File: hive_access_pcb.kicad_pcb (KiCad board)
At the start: 2 copper layers, 43 parts, among them J1 Door Reader, J2 Snub Enable, J3 Relay Mode Select, J4 Relay Voltage Select, J5 Power In, J6 Exit Sensor, K1 SANYOU_SRD_Form_C, P1 Door Latch Solenoid Out, P2 External Reset, P3 Door Closed Sensor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

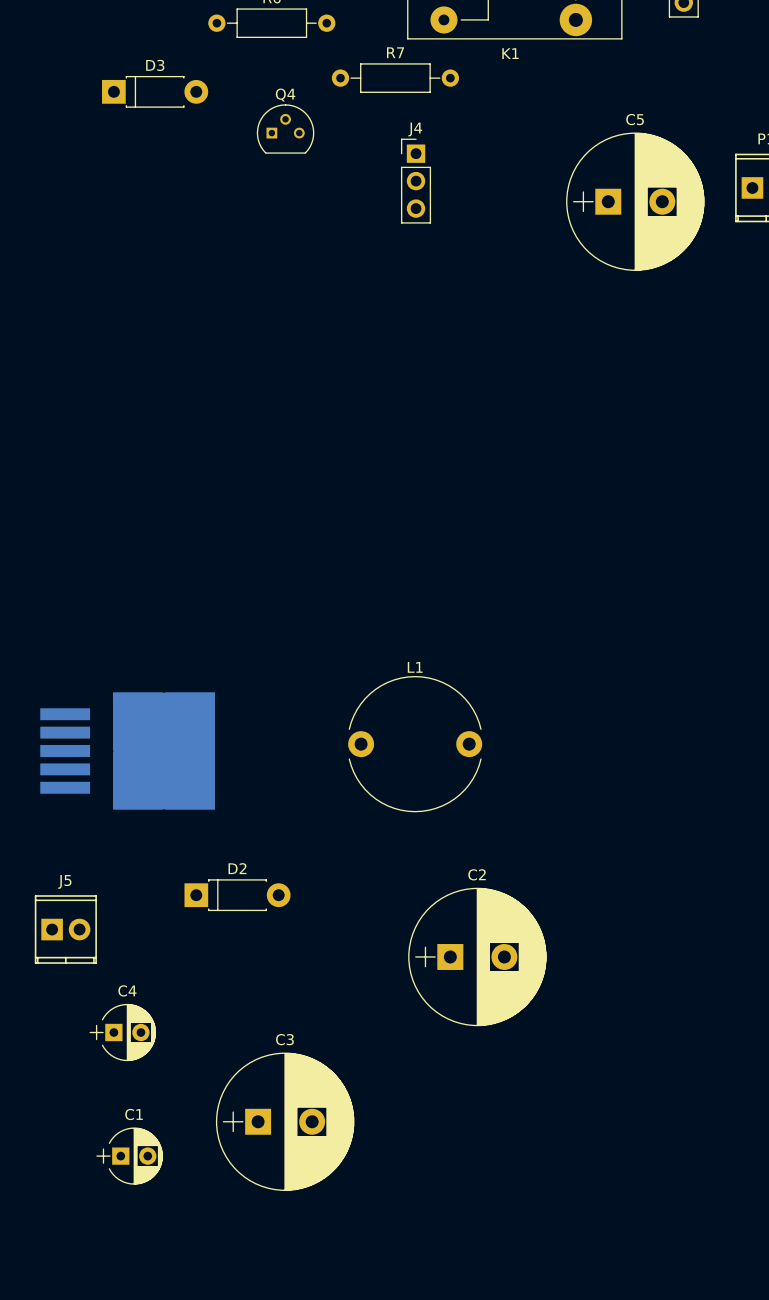
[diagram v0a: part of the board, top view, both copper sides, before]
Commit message: All components correctly sized, except connectors.  Need to check TO-92 pinouts.
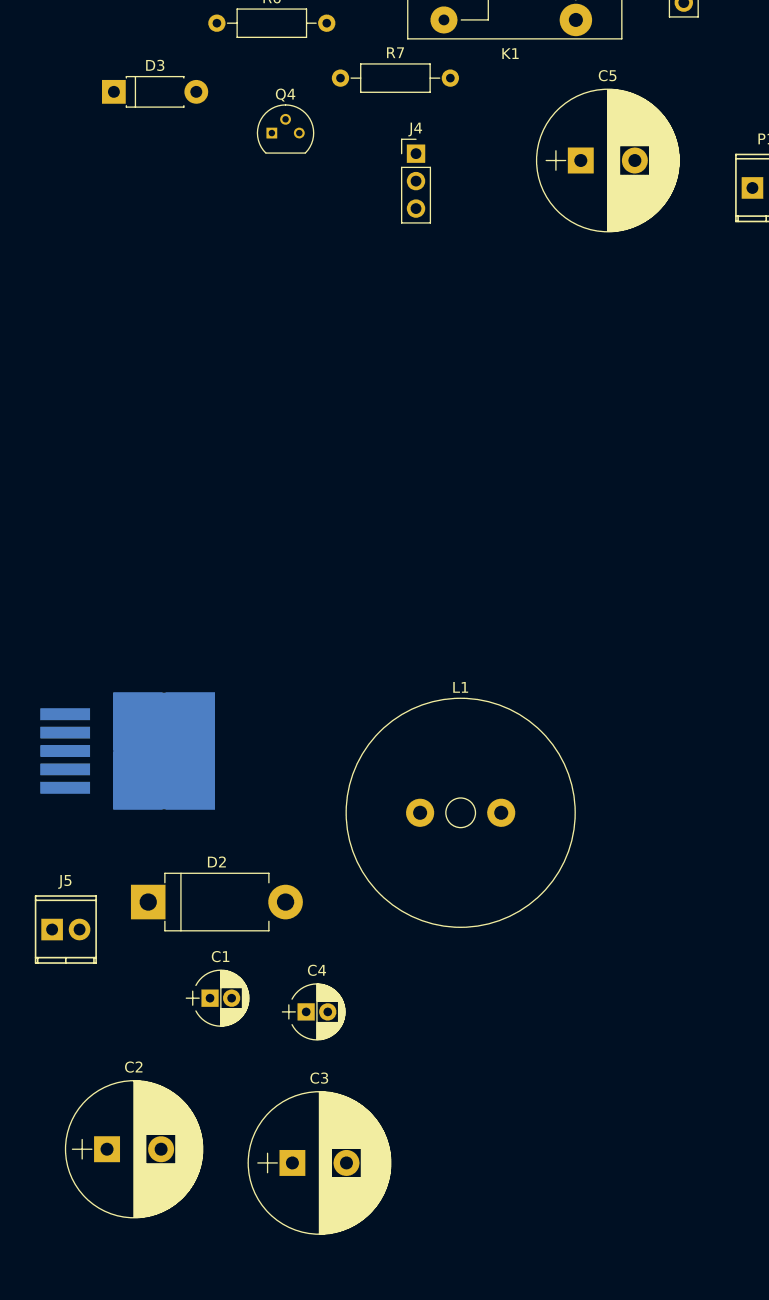
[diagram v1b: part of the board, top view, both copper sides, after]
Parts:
- C1, C4: footprint Capacitors_THT:CP_Radial_D5.0mm_P2.50mm -> Capacitors_THT:CP_Radial_D5.0mm_P2.00mm
- C3, C5: footprint Capacitors_THT:CP_Radial_D12.5mm_P5.00mm -> Capacitors_THT:CP_Radial_D13.0mm_P5.00mm
- D2: footprint Diodes_THT:D_DO-41_SOD81_P7.62mm_Horizontal -> Diodes_THT:D_DO-201AD_P12.70mm_Horizontal
- L1: footprint Inductors_THT:L_Radial_D12.0mm_P10.00mm_Neosid_SD12_style1 -> Inductor:L_Radial_D21.0mm_P7.5mm
- moved C2 36.4 mm to (191.1, 141.0)
- moved C4 17.9 mm to (209.6, 128.3)
- moved C1 16.8 mm to (200.7, 127.0)
- moved L1 6.63 mm to (216.5, 109.9)
- moved C3 4.96 mm to (208.3, 142.2)
- moved C5 4.58 mm to (234.9, 49.5)
- moved D2 4.49 mm to (194.9, 118.1)

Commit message: First draft of the circuit board.
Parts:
- moved J1 193.5 mm to (233.7, 55.9), turned to 180 degrees
- moved R5 192.4 mm to (252.7, 72.4), turned to 180 degrees
- moved R4 192.4 mm to (252.7, 77.5), turned to 180 degrees
- moved C6 187.7 mm to (221.6, 65.4)
- moved R1 186.2 mm to (228.6, 77.5)
- moved R2 184.8 mm to (228.6, 72.4)
- moved Q3 181.9 mm to (240.7, 66.0)
- moved U3 175.2 mm to (222.2, 75.6)
- moved Q2 174.5 mm to (233.0, 66.0)
- moved R9 160.8 mm to (230.5, 118.7), turned to 270 degrees
- moved P2 152.1 mm to (239.4, 137.2)
- moved U4 150.3 mm to (237.5, 99.7)
- moved U2 148.5 mm to (238.1, 125.1), turned to 90 degrees
- moved P3 106.6 mm to (216.5, 64.8), turned to 180 degrees
- moved J3 92.5 mm to (166.4, 76.8), turned to 270 degrees
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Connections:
- U3 pad 13: /WIEGAND_BEEP -> /WIEGAND_LIGHT
- U3 pad 14: /WIEGAND_LIGHT -> /WIEGAND_BEEP
- U4 pad 5: /WEMOS_D1 -> /WEMOS_D0
- U4 pad 6: /WEMOS_D0 -> /WEMOS_D1
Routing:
- net GND: track 0.00 -> 525.7 mm, vias 0 -> 12
- net +5V: track 0.00 -> 287.2 mm, vias 0 -> 4
- net +12V: track 0.00 -> 245.2 mm, vias 0 -> 4
- net +3V3: track 0.00 -> 223.4 mm, vias 0 -> 6
- net /ONE_WIRE: track 0.00 -> 104.4 mm, vias 0 -> 2
- net /WEMOS_TRIG: track 0.00 -> 87.2 mm
- net /WEMOS_ECHO: track 0.00 -> 75.5 mm
- net /~RST: track 0.00 -> 59.1 mm
- net /RELAY_POWER: track 0.00 -> 44.4 mm
- net /HC_TRIG: track 0.00 -> 42.1 mm
- net /WEMOS_D1: track 0.00 -> 42.0 mm
- net /DOOR_SENSOR: track 0.00 -> 41.8 mm
- net /WEMOS_D0: track 0.00 -> 40.7 mm
- net /RELAY_CONN: track 0.00 -> 37.8 mm
- net /WIEGAND_D1: track 0.00 -> 35.6 mm
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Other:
- net class Default: clearance 0.2 -> 0.2032; trace_width 0.25 -> 0.254; via_dia 0.6 -> 2.54; via_drill 0.4 -> 1.27
- net class Lesser Power added: clearance 0.2032, trace_width 1.016, via_dia 1.905, via_drill 1.016
- net class Power added: clearance 0.2032, trace_width 1.524, via_dia 1.905, via_drill 1.016
- rule trace_clearance: 0.2 -> 0.2032

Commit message: Design rule tweaks.
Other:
- board outline added: 139.1 x 111.8 mm
- net class Default: clearance 0.2032 -> 0.2286; via_dia 2.54 -> 1.905; via_drill 1.27 -> 1.016
- net class Lesser Power: clearance 0.2032 -> 0.2286
- net class Power: clearance 0.2032 -> 0.2286; via_dia 1.905 -> 2.286; via_drill 1.016 -> 1.27
- rule trace_clearance: 0.2032 -> 0.2286
- rule trace_min: 0.2 -> 0.2032
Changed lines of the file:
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@@
     (area 0 0 0 0)
     (thickness 1.6)
-    (drawings 0)
-    (tracks 462)
+    (drawings 4)
+    (tracks 464)
     (zones 0)
     (modules 43)
@@
     (user_trace_width 0.635)
     (user_trace_width 1.1176)
-    (trace_clearance 0.2032)
+    (trace_clearance 0.2286)
     (zone_clearance 0.508)
     (zone_45_only no)
-    (trace_min 0.2)
+    (trace_min 0.2032)
     (segment_width 0.2)
     (edge_width 0.15)
-    (via_size 2.54)
-    (via_drill 1.27)
+    (via_size 1.905)
+    (via_drill 1.016)
     (via_min_size 0.4)
     (via_min_drill 0.3)
@@
   (net 41 "Net-(K1-Pad3)")
   (net_class Default "This is the default net class."
-    (clearance 0.2032)
+    (clearance 0.2286)
     (trace_width 0.254)
-    (via_dia 2.54)
-    (via_drill 1.27)
+    (via_dia 1.905)
+    (via_drill 1.016)
     (uvia_dia 0.3)
     (uvia_drill 0.1)
@@
   )
   (net_class "Lesser Power" ""
-    (clearance 0.2032)
+    (clearance 0.2286)
     (trace_width 1.016)
     (via_dia 1.905)
@@
   )
   (net_class Power ""
-    (clearance 0.2032)
+    (clearance 0.2286)
     (trace_width 1.524)
-    (via_dia 1.905)
-    (via_drill 1.016)
+    (via_dia 2.286)
+    (via_drill 1.27)
     (uvia_dia 0.3)
     (uvia_drill 0.1)
@@
     )
   )
+  (gr_line (start 116.205 33.655) (end 255.27 33.655) (angle 90) (layer Edge.Cuts) (width 0.15))
+  (gr_line (start 116.205 145.415) (end 116.205 33.655) (angle 90) (layer Edge.Cuts) (width 0.15))
+  (gr_line (start 255.27 145.415) (end 116.205 145.415) (angle 90) (layer Edge.Cuts) (width 0.15))
+  (gr_line (start 255.27 33.655) (end 255.27 145.415) (angle 90) (layer Edge.Cuts) (width 0.15))
   (via (at 222.885 83.185) (size 1.905) (drill 1.016) (layers F.Cu B.Cu) (net 1))
-  (segment (start 252.73 77.47) (end 252.73 78.74) (width 1.016) (layer B.Cu) (net 1) (status 400000))
+  (segment (start 252.73 77.47) (end 252.73 78.74) (width 1.016) (layer B.Cu) (net 1))
   (segment (start 248.285 83.185) (end 252.73 78.74) (width 1.016) (layer B.Cu) (net 1))
   (via (at 248.285 83.185) (size 1.905) (drill 1.016) (layers F.Cu B.Cu) (net 1))
@@
   (segment (start 196.85 137.795) (end 196.85 133.985) (width 0.254) (layer B.Cu) (net 4))
   (segment (start 196.85 133.985) (end 202.565 128.27) (width 0.254) (layer B.Cu) (net 4))
+  (segment (start 250.825 109.855) (end 250.825 110.49) (width 0.254) (layer B.Cu) (net 5))
+  (segment (start 250.825 110.49) (end 240.03 121.285) (width 0.254) (layer B.Cu) (net 5))
   (segment (start 220.345 130.81) (end 215.265 130.81) (width 0.254) (layer B.Cu) (net 5))
   (segment (start 250.825 106.68) (end 250.825 107.95) (width 0.254) (layer B.Cu) (net 5))
-  (segment (start 240.03 120.65) (end 240.03 127) (width 0.254) (layer B.Cu) (net 5))
+  (segment (start 240.03 121.285) (end 240.03 127) (width 0.254) (layer B.Cu) (net 5))
   (segment (start 240.03 127) (end 236.22 130.81) (width 0.254) (layer B.Cu) (net 5))
   (segment (start 236.22 130.81) (end 220.345 130.81) (width 0.254) (layer B.Cu) (net 5))
-  (segment (start 250.825 109.855) (end 240.03 120.65) (width 0.254) (layer B.Cu) (net 5))
   (segment (start 250.825 107.95) (end 250.825 109.855) (width 0.254) (layer B.Cu) (net 5))
   (segment (start 250.825 106.045) (end 249.555 104.775) (width 0.254) (layer B.Cu) (net 5))
@@
   (segment (start 217.805 85.09) (end 217.805 79.375) (width 0.254) (layer B.Cu) (net 27))
   (segment (start 219.075 86.36) (end 217.805 85.09) (width 0.254) (layer B.Cu) (net 27))
+  (via (at 220.345 123.825) (size 1.905) (drill 1.016) (layers F.Cu B.Cu) (net 28))
+  (segment (start 220.345 123.825) (end 228.6 123.825) (width 0.254) (layer B.Cu) (net 28))
+  (segment (start 220.345 92.71) (end 220.345 123.825) (width 0.254) (layer F.Cu) (net 28))
+  (segment (start 228.6 123.825) (end 230.505 123.825) (width 0.254) (layer B.Cu) (net 28))
+  (via (at 220.345 92.71) (size 1.905) (drill 1.016) (layers F.Cu B.Cu) (net 28))
+  (segment (start 219.075 91.44) (end 220.345 92.71) (width 0.254) (layer B.Cu) (net 28))
   (segment (start 241.935 98.425) (end 247.65 98.425) (width 0.254) (layer B.Cu) (net 28))
-  (segment (start 220.345 93.98) (end 224.79 98.425) (width 0.254) (layer B.Cu) (net 28))
-  (segment (start 224.79 98.425) (end 241.935 98.425) (width 0.254) (layer B.Cu) (net 28))
-  (segment (start 220.345 92.71) (end 220.345 93.98) (width 0.254) (layer B.Cu) (net 28))
   (segment (start 247.65 98.425) (end 248.92 99.695) (width 0.254) (layer B.Cu) (net 28))
+  (segment (start 220.345 92.71) (end 220.345 93.98) (width 0.254) (layer B.Cu) (net 28))
+  (segment (start 224.79 98.425) (end 241.935 98.425) (width 0.254) (layer B.Cu) (net 28))
+  (segment (start 220.345 93.98) (end 224.79 98.425) (width 0.254) (layer B.Cu) (net 28))
   (segment (start 230.505 125.73) (end 230.505 123.825) (width 0.254) (layer B.Cu) (net 28))
+  (segment (start 230.505 125.73) (end 230.505 127) (width 0.254) (layer B.Cu) (net 28))
+  (segment (start 230.505 127) (end 230.505 128.905) (width 0.254) (layer B.Cu) (net 28))
   (segment (start 233.68 123.825) (end 230.505 123.825) (width 0.254) (layer B.Cu) (net 28))
-  (segment (start 230.505 123.825) (end 228.6 123.825) (width 0.254) (layer B.Cu) (net 28))
   (segment (start 219.55 76.2) (end 218.44 76.2) (width 0.254) (layer B.Cu) (net 28))
   (segment (start 218.44 76.2) (end 217.17 77.47) (width 0.254) (layer B.Cu) (net 28))
   (segment (start 217.17 77.47) (end 217.17 89.535) (width 0.254) (layer B.Cu) (net 28))
-  (segment (start 217.17 89.535) (end 220.345 92.71) (width 0.254) (layer B.Cu) (net 28))
-  (via (at 220.345 92.71) (size 2.54) (drill 1.27) (layers F.Cu B.Cu) (net 28))
-  (segment (start 220.345 92.71) (end 220.345 123.825) (width 0.254) (layer F.Cu) (net 28))
-  (via (at 220.345 123.825) (size 2.54) (drill 1.27) (layers F.Cu B.Cu) (net 28))
-  (segment (start 220.345 123.825) (end 228.6 123.825) (width 0.254) (layer B.Cu) (net 28))
-  (segment (start 230.505 125.73) (end 230.505 127) (width 0.254) (layer B.Cu) (net 28))
+  (segment (start 217.17 89.535) (end 219.075 91.44) (width 0.254) (layer B.Cu) (net 28))
   (segment (start 236.855 123.825) (end 233.68 123.825) (width 0.254) (layer B.Cu) (net 28))
-  (segment (start 230.505 127) (end 230.505 128.905) (width 0.254) (layer B.Cu) (net 28))
 )
